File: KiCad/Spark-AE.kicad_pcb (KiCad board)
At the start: 2 copper layers, 1 part

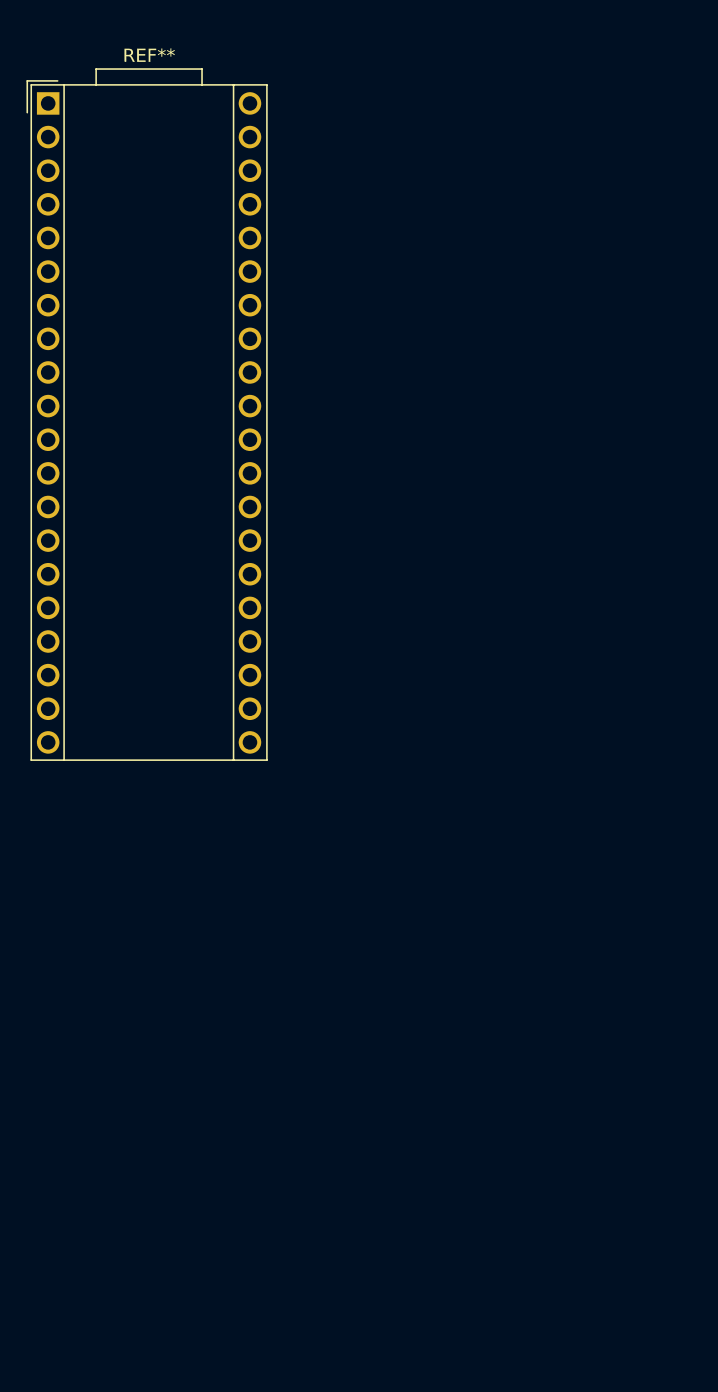
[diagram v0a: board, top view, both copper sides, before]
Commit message: Roughing out the basic edges and control layout.
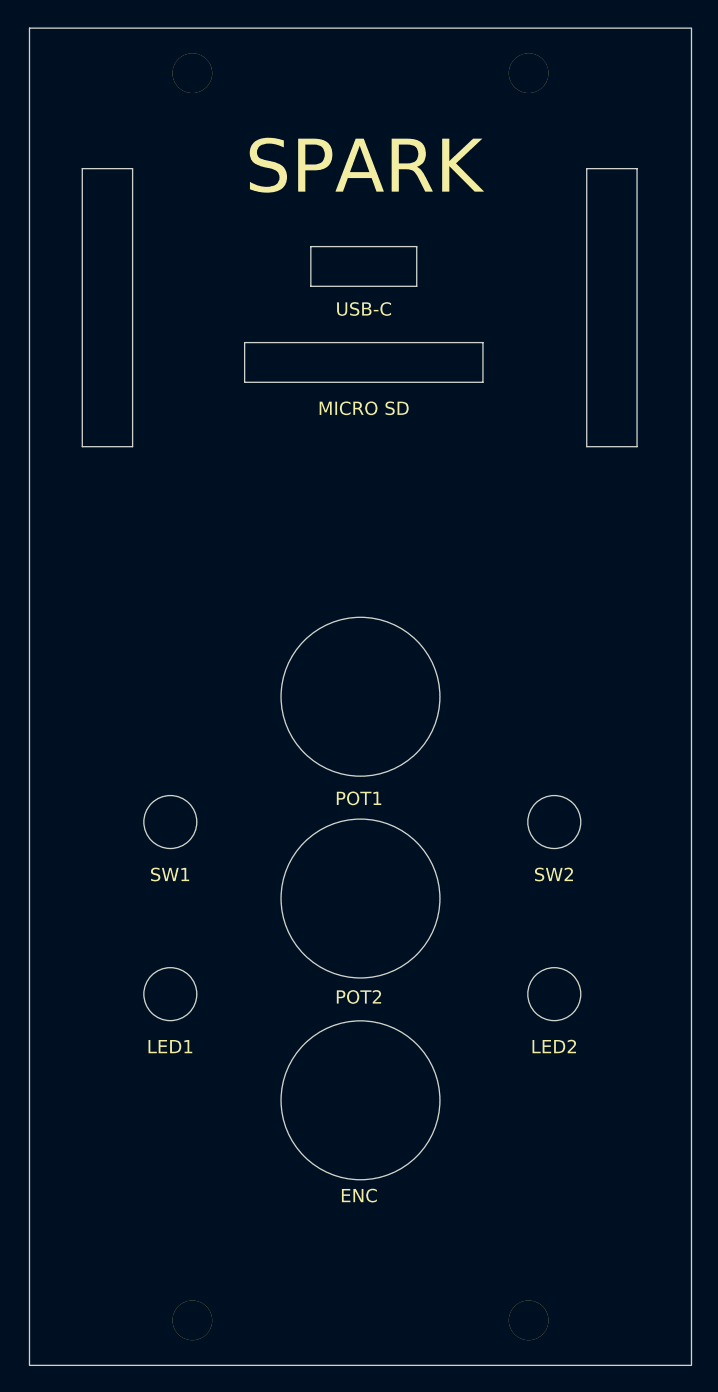
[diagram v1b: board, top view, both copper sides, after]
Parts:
- removed the REF** at (92.0, 51.0)
- added REF**: AE_2U_PANEL, clectric-diy:AE_2U_PANEL, F.Cu at (84.6, 151.5)
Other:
- board outline added: 50 x 101 mm
- copper layers 2 -> 4
- board text added: "ENC"
- board text added: "LED1"
- board text added: "LED2"
- board text added: "MICRO SD"
- board text added: "POT1"
- board text added: "POT2"
- board text added: "SPARK"
- board text added: "SW1"
- board text added: "SW2"
- board text added: "USB-C"

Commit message: removed led holes in favor of transparent pots
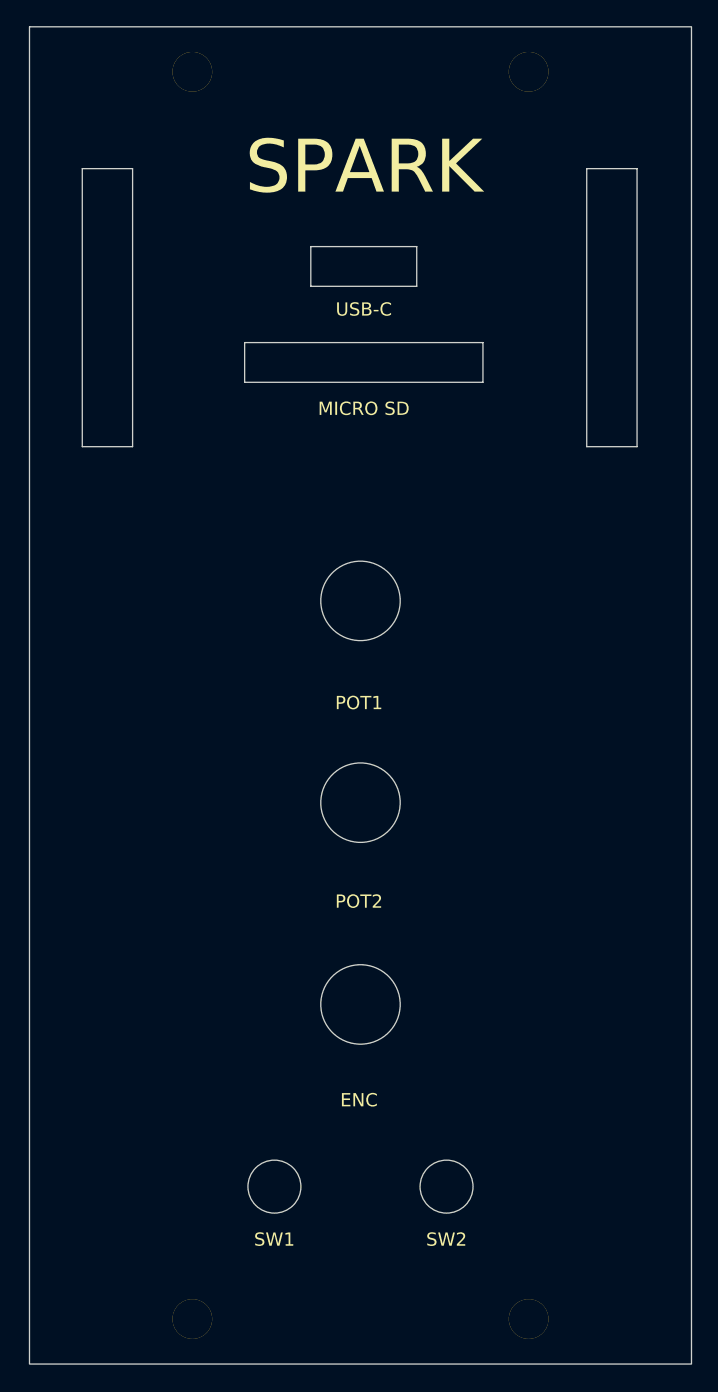
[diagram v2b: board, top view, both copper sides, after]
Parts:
- moved REF** 0.10 mm to (84.6, 151.4)
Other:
- board text removed: "LED1"
- board text removed: "LED2"
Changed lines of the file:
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@@
 		(13 "F.Paste" user)
 		(15 "B.Paste" user)
-		(5 "F.SilkS" user)
-		(7 "B.SilkS" user)
+		(5 "F.SilkS" user "F.Silkscreen")
+		(7 "B.SilkS" user "B.Silkscreen")
 		(1 "F.Mask" user)
 		(3 "B.Mask" user)
 		(25 "Edge.Cuts" user)
 		(27 "Margin" user)
-		(31 "F.CrtYd" user)
-		(29 "B.CrtYd" user)
+		(31 "F.CrtYd" user "F.Courtyard")
+		(29 "B.CrtYd" user "B.Courtyard")
 		(35 "F.Fab" user)
 	)
@@
 	(footprint "clectric-diy:AE_2U_PANEL"
 		(layer "F.Cu")
-		(at 84.5875 151.5125)
+		(at 84.5875 151.4125)
 		(property "Reference" "REF**"
 			(at 0 -0.5 0)
@@
 	)
 	(gr_circle
-		(center 101.225 118.275)
-		(end 103.225 118.275)
-		(stroke
-			(width 0.0381)
-			(type solid)
-		)
-		(fill no)
-		(layer "Edge.Cuts")
-	)
-	(gr_circle
-		(center 115.5875 126.2925)
-		(end 121.5875 126.2925)
-		(stroke
-			(width 0.0381)
-			(type solid)
-		)
-		(fill no)
-		(layer "Edge.Cuts")
-	)
-	(gr_circle
-		(center 130.225 118.275)
-		(end 132.225 118.275)
+		(center 115.5875 119.0525)
+		(end 118.5875 119.0525)
 		(stroke
 			(width 0.0381)
@@
 	)
 	(gr_circle
-		(center 130.225 105.275)
-		(end 132.225 105.275)
+		(center 122.0875 132.8125)
+		(end 124.0875 132.8125)
 		(stroke
 			(width 0.0381)
@@
 	)
 	(gr_circle
-		(center 115.5875 95.8125)
-		(end 121.5875 95.8125)
+		(center 115.5875 88.5725)
+		(end 118.5875 88.5725)
 		(stroke
 			(width 0.0381)
@@
 	)
 	(gr_rect
-		(start 98.375 55.925)
-		(end 94.575 76.925)
+		(start 94.575 55.925)
+		(end 98.375 76.925)
 		(stroke
 			(width 0.0381)
@@
 	)
 	(gr_circle
-		(center 101.225 105.275)
-		(end 103.225 105.275)
+		(center 109.0875 132.8125)
+		(end 111.0875 132.8125)
 		(stroke
 			(width 0.0381)
@@
 	)
 	(gr_circle
-		(center 115.5875 111.0525)
-		(end 121.5875 111.0525)
+		(center 115.5875 103.8125)
+		(end 118.5875 103.8125)
 		(stroke
 			(width 0.0381)
@@
 	)
 	(gr_text "POT2"
-		(at 115.475 118.525 0)
+		(at 115.475 111.285 0)
 		(layer "F.SilkS")
 		(effects
@@
 	)
 	(gr_text "SW2"
-		(at 130.225 109.275 0)
-		(layer "F.SilkS")
-		(effects
-			(font
-				(size 1 1)
-				(thickness 0.125)
-			)
-		)
-	)
-	(gr_text "LED1"
-		(at 101.225 122.275 0)
+		(at 122.0875 136.8125 0)
 		(layer "F.SilkS")
 		(effects
@@
 	)
 	(gr_text "POT1"
-		(at 115.475 103.525 0)
+		(at 115.475 96.285 0)
 		(layer "F.SilkS")
 		(effects
@@
 	)
 	(gr_text "ENC"
-		(at 115.475 133.525 0)
-		(layer "F.SilkS")
-		(effects
-			(font
-				(size 1 1)
-				(thickness 0.125)
-			)
-		)
-	)
-	(gr_text "LED2"
-		(at 130.225 122.275 0)
+		(at 115.475 126.285 0)
 		(layer "F.SilkS")
 		(effects
@@
 	)
 	(gr_text "SW1"
-		(at 101.225 109.275 0)
+		(at 109.0875 136.8125 0)
 		(layer "F.SilkS")
 		(effects
@@
 	)
 	(group ""
-		(members "107dfc05-5d9c-4b52-ae93-4c4989ac0309" "73417f26-f35c-4e41-bfa8-d11fc95d58fd"
-			"e1319850-e188-4a0f-aeae-5becc3f31631" "e7300c64-82ab-4c78-975c-5fd518bbfe55"
-		)
+		(members "6d0a3104-8483-4dae-b45d-bf11ce57599a" "bc85fd9a-2dc7-48e5-9c8d-aea13b2ea052")
 	)
 	(group ""
-		(members "674cf54a-7b47-4763-9a85-47c8b6ba80f2" "88aa30bf-a09c-47d6-8f66-543a711b2950")
+		(members "e1319850-e188-4a0f-aeae-5becc3f31631" "e7300c64-82ab-4c78-975c-5fd518bbfe55")
 	)
 	(group ""
-		(members "65142baa-0012-4ac3-84b8-cc2549c80d3a" "6d0a3104-8483-4dae-b45d-bf11ce57599a"
-			"bc85fd9a-2dc7-48e5-9c8d-aea13b2ea052" "d09174a8-bf1d-4829-83c1-5999c03ae60b"
-		)
-	)
-	(group ""
-		(members "281cc032-5aba-407d-a67d-36dfd9098330" "4809e407-e467-424a-a81a-ba95a5a363f0")
-	)
-	(group ""
-		(members "38064fc3-8f43-425b-a2c1-522743cf0862" "3e7d8bae-4a24-4759-a8a0-d1f29291c46c"
-			"796d6d3f-7bf0-4afc-a6ba-773a705f6e27" "9e3886ec-699a-4709-895a-0b800ce282a8"
-		)
-	)
-	(group ""
-		(members "30f8df87-a1f7-46b9-98fe-035d254694ee" "c6301a97-7989-494d-add6-334b4ccd2ffe"
-			"ecdf6711-0909-49e7-8060-622a6367326d"
-		)
+		(members "46469b11-1c55-4afa-89c9-9d31744dcc15" "658b08ae-60e7-42cc-ad00-90a8e2e7780c")
 	)
 	(embedded_fonts no)
